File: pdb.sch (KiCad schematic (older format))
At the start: 0 parts

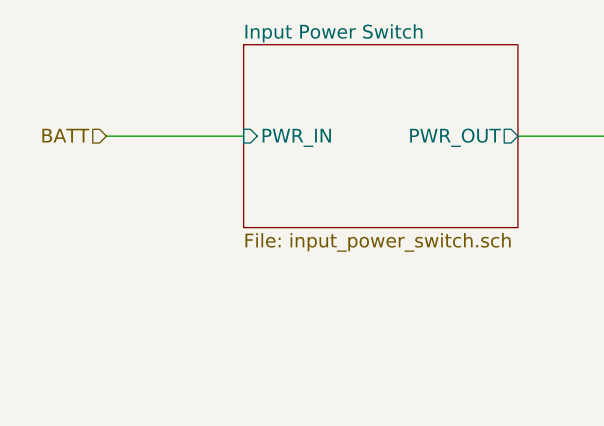
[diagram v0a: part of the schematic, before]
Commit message: add input power switching circuit
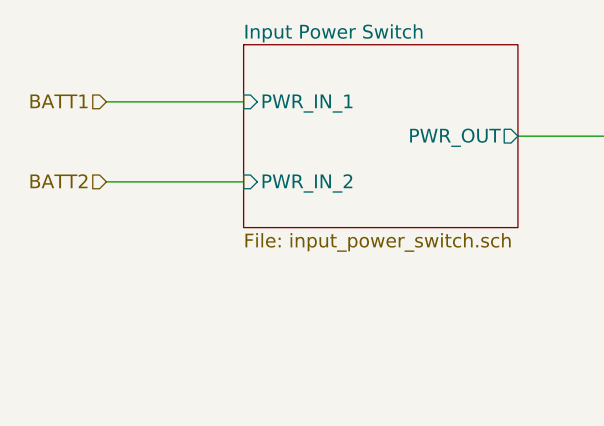
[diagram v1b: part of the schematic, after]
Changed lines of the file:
@@
 LIBS:ltc1473
 LIBS:agg-kicad
+LIBS:nmos_sssgd
+LIBS:pdb-cache
 EELAYER 25 0
 EELAYER END
@@
 F1 "input_power_switch.sch" 60
 F2 "PWR_OUT" O R 3450 3200 60
-F3 "PWR_IN" I L 2250 3200 60
+F3 "PWR_IN_1" I L 2250 3050 60
+F4 "PWR_IN_2" I L 2250 3400 60
 $EndSheet
 $Sheet
@@
 Wire Wire Line
 	7850 4400 8300 4400
-Text HLabel 1650 3200 0    60   Input ~ 0
-BATT
+Text HLabel 1650 3050 0    60   Input ~ 0
+BATT1
 Wire Wire Line
-	1650 3200 2250 3200
+	1650 3050 2250 3050
+Text HLabel 1650 3400 0    60   Input ~ 0
+BATT2
+Wire Wire Line
+	1650 3400 2250 3400
 $EndSCHEMATC
